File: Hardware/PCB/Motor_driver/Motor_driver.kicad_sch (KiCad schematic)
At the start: 87 parts, among them IC1 A89307KETSR-J, IC2 STM32L412KBT6, J1 ENCODER, J2 USB_C, J3 PAD_MOTEUR, J4 Debug, J5 Conn_01x01_Pin, J6 Conn_01x01_Pin, J7 Conn_01x01_Pin, J8 Conn_01x01_Pin

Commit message: update PCB, check driver BLDC
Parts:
- removed C22: 22µF, Capacitor_SMD:C_0603_1608Metric, symbol Device:C_Small
- removed C7, C8: 15µF, symbol Device:C_Polarized_Small
- removed D3: D_Zener 45V, symbol Device:D_Zener
- removed R1: 0.025, Resistor_SMD:R_0603_1608Metric, symbol Device:R
- removed R11, R13: 1, symbol Device:R
- removed R12, R14, R19, R20, R23: 0, symbol Device:R
- removed R21: 1k, symbol Device:R
- removed SQJ746ELP1, SQJ746ELP2, SQJ746ELP3: ~, Package_SO:PowerPAK_SO-8_Dual, symbol Custom:SQJ746ELP
- removed TP5: GATE C, TestPoint:TestPoint_Pad_D1.5mm, symbol Connector:TestPoint
- removed TP6: GATE B, TestPoint:TestPoint_Pad_D1.5mm, symbol Connector:TestPoint
- removed TP7: GATE A, TestPoint:TestPoint_Pad_D1.5mm, symbol Connector:TestPoint
- added J9: Conn_ST_STDC14, symbol Connector:Conn_ST_STDC14
- added R11: R_Shunt, symbol Device:R_Shunt
- C1, C2, C3: value 22µF -> 220n
- C15: value 4.7µF -> 4u7
- D1: MPN (none) -> 150060RS55040
- R2: value 200 -> 1k7
- R22: value 0 -> 10k; footprint (none) -> Resistor_SMD:R_0603_1608Metric
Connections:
- net +3.3V: now also R2.2, R22.2
- net GND: now also R11.4; no longer D1.1 (K), IC1.28 (SENN)
- net LSS: now also R11.1; no longer IC1.1 (SENP)
- net SA: no longer IC1.8 (SA), R22.2
- net SB: no longer IC1.10 (SB)
- net SC: no longer IC1.12 (SC)
- net arm_bridge_C/GHx: now reaches IC1.13 (GHC)
- net arm_bridge_A/GHx: now reaches IC1.9 (GHA)
- net at R22.1: now also D1.1 (K), IC1.26 (FAULT)
- net arm_bridge_B/GHx: now reaches IC1.11 (GHB)
- new net: J9.5 (GND), J9.7 (GND)
- new net SENN: IC1.28 (SENN), R11.3
- new net SENP: IC1.1 (SENP), R11.2
- new net arm_bridge_A/Sx: IC1.8 (SA)
- new net arm_bridge_B/Sx: IC1.10 (SB)
- new net arm_bridge_C/Sx: IC1.12 (SC)
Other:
- added sheet arm_bridge_A (arm_bridge.kicad_sch)
- added sheet arm_bridge_B (arm_bridge.kicad_sch)
- added sheet arm_bridge_C (arm_bridge.kicad_sch)
- moved on the sheet: C1, C2, C21, C3, D1, R2

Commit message: clean schematic
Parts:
- removed C17: 100nF, Capacitor_SMD:C_0603_1608Metric, symbol Device:C_Small
- removed IC2: STM32L412KBT6, SamacSys_Parts:QFP80P900X900X160-32N, symbol SamacSys_Parts:STM32L412KBT6
- removed J5, J6, J7, J8: Conn_01x01_Pin, MountingHole:MountingHole_3.2mm_M3_Pad_TopBottom, symbol Connector:Conn_01x01_Pin
- removed R17, R18, R6: 10k, Resistor_SMD:R_0603_1608Metric, symbol Device:R
- removed S1: 430181038816, SamacSys_Parts:430181038816, symbol SamacSys_Parts:430181038816
- removed TP10: BRAKE, TestPoint:TestPoint_Pad_D1.5mm, symbol Connector:TestPoint
- removed TP3: RX, TestPoint:TestPoint_Pad_D1.5mm, symbol Connector:TestPoint
- removed TP4: TX, TestPoint:TestPoint_Pad_D1.5mm, symbol Connector:TestPoint
- added H1, H2, H3, H4: MountingHole_Pad, symbol Mechanical:MountingHole_Pad
- added R1, R17: 10k, symbol Device:R_Small
- added R6: R_Small, symbol Device:R_Small
- added TP23: BRAKE, TestPoint:TestPoint_Pad_D1.5mm, symbol Connector:TestPoint
- added U2: STM32L412KBTx, Package_QFP:LQFP-32_7x7mm_P0.8mm, symbol MCU_ST_STM32L4:STM32L412KBTx
- C11: value 1µF -> 1u
- C12, C14, C4: value 4.7µF -> 4u7
- C13, C19: value 22µF -> 22u
- C16: value 100nF -> 100n
- C18: value 10µF -> 10u
- C20: value 15pF -> 15p
- C9: value 220µF -> 220u
- R3: value 5.6k -> 5k6
- renumbered Oscillator1 to Osc1
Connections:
- net +3.3V: now also J9.3 (VCC), R1.2, R17.1, R6.1, U2.1 (VDD), U2.17 (VDD), U2.5 (VDDA)
- net A: now also U2.6 (PA0)
- net B: now also U2.7 (PA1)
- net BRAKE: now also TP23.1, U2.13 (PA7)
- net DIR: now also U2.12 (PA6)
- net GND: now also J9.11 (GNDDetect), J9.5 (GND), J9.7 (GND), H1.1, H2.1, H3.1, H4.1, U2.16 (VSS), U2.32 (VSS)
- net GPIO3: now also U2.10 (PA4)
- net PA11: now also U2.21 (PA11)
- net PWM: now also U2.11 (PA5)
- net RX: now also U2.30 (PB7)
- net SCL: now also R15.1, TP1.1, U2.19 (PA9); no longer R16.1, TP2.1
- net SDA: now also R16.1, TP2.1, U2.20 (PA10); no longer R15.1, TP1.1
- net SWCLK: now also U2.24 (PA14)
- net SWDIO: now also U2.23 (PA13)
- net SWO: now also U2.26 (PB3)
- net TX: now also U2.29 (PB6)
- net X: now also U2.9 (PA3)
- net at S3.1: now also R1.1
- net at S3.3 (2): now also U2.15 (PB1)
- net at S3.4 (1): now also U2.14 (PB0)
- net at S3.2: now also R17.2
- new net: R6.2, U2.4 (NRST)
- no-connect marks 16 -> 10
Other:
- moved on the sheet: C1, C10, C11, C12, C13, C14, C15, C16, C18, C19, C2, C20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

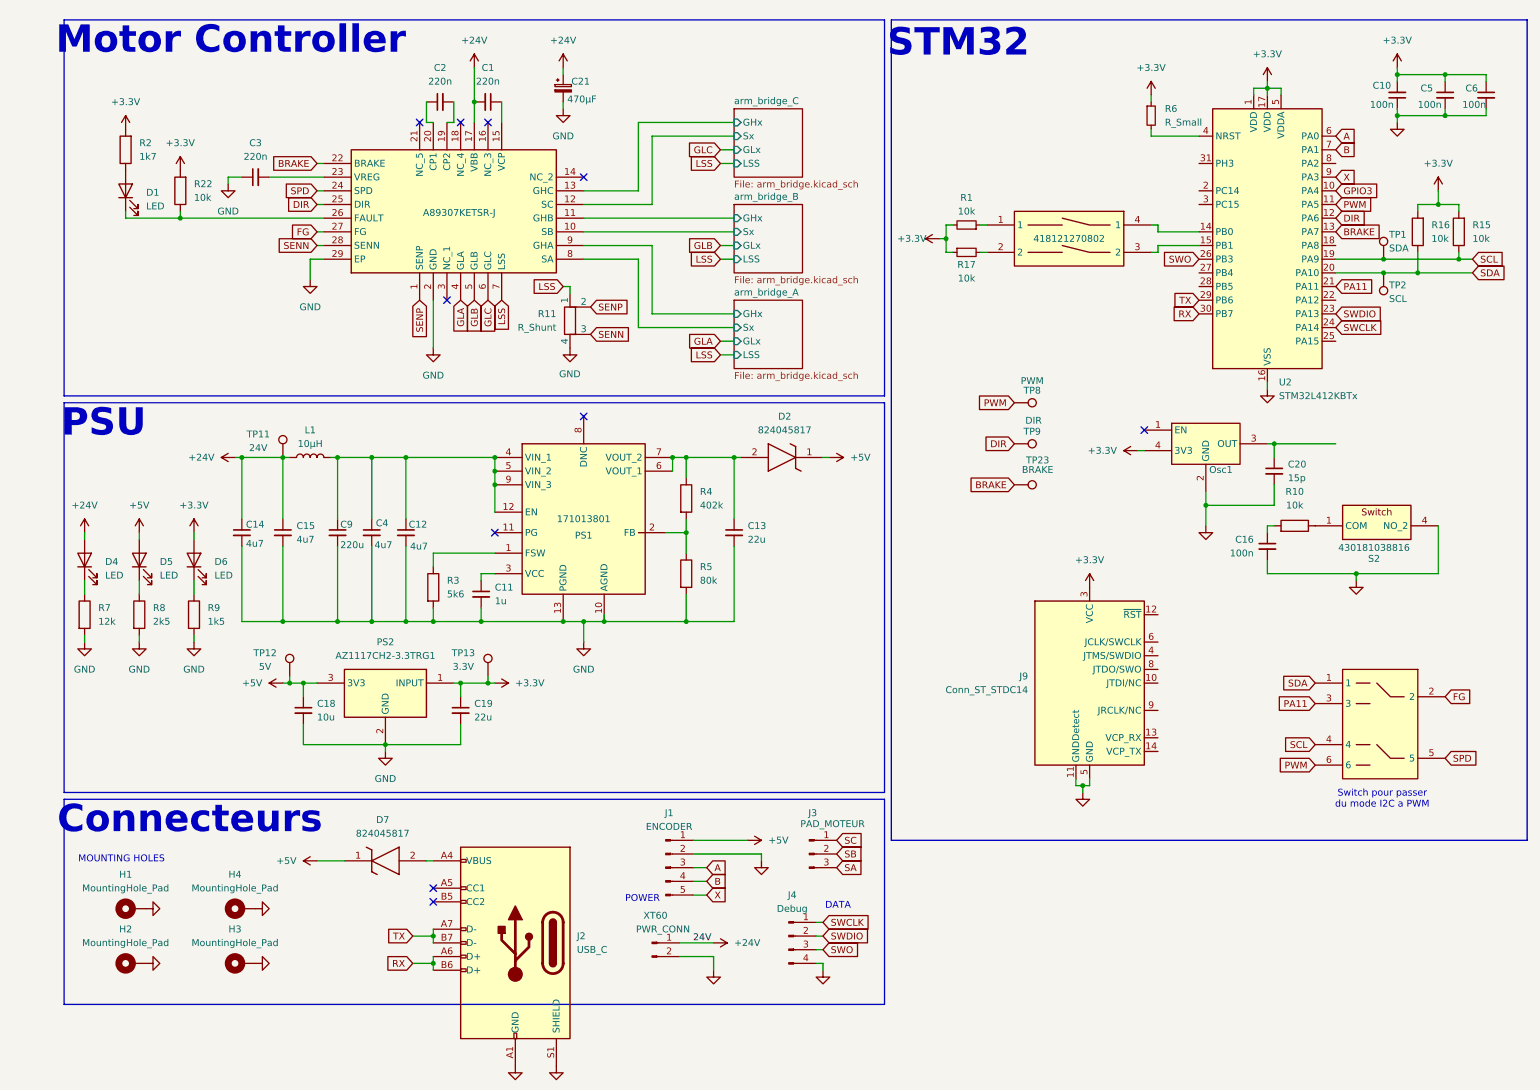
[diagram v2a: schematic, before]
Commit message: update schematic
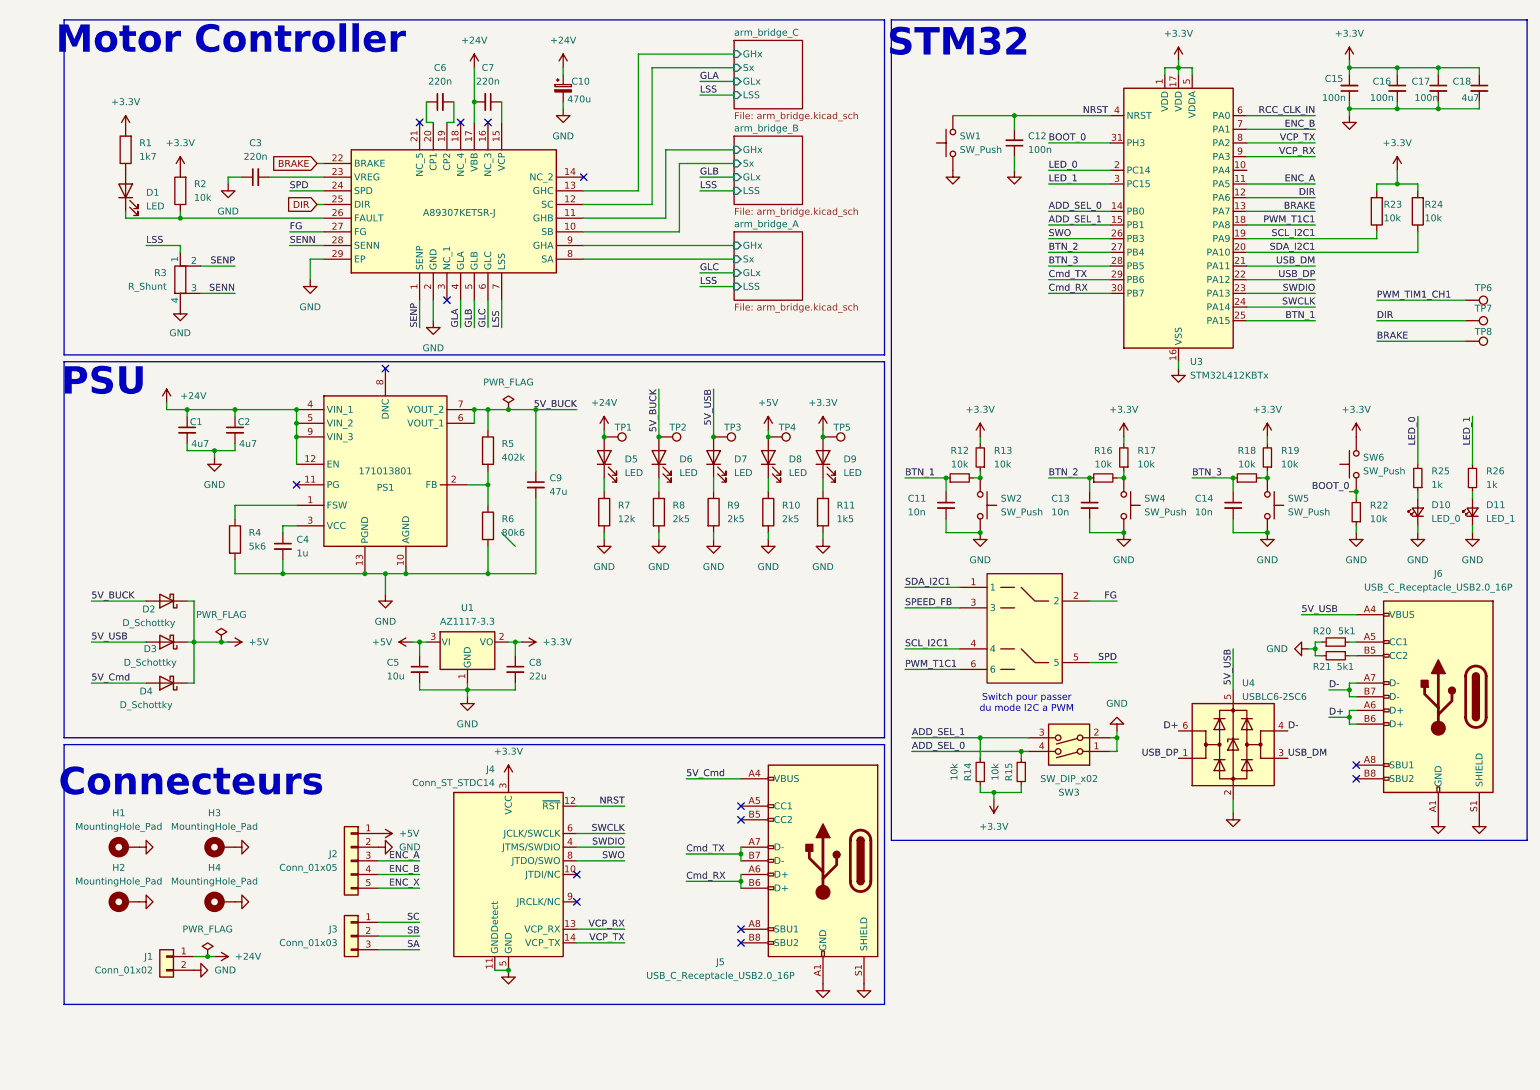
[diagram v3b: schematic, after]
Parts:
- removed C15, C4: 4u7, Capacitor_SMD:C_0603_1608Metric, symbol Device:C_Small
- removed C16: 100n, Capacitor_SMD:C_0603_1608Metric, symbol Device:C_Small
- removed C20: 15p, Capacitor_SMD:C_0603_1608Metric, symbol Device:C_Small
- removed C9: 220u, Capacitor_SMD:C_0603_1608Metric, symbol Device:C_Small
- removed D2, D7: 824045817, SamacSys_Parts:824045817, symbol SamacSys_Parts:824045817
- removed J1: ENCODER, Connector_JST:JST_SH_SM05B-SRSS-TB_1x05-1MP_P1.00mm_Horizontal, symbol Connector:Conn_01x05_Pin
- removed J2: USB_C, Connector_USB:USB_C_Receptacle_GCT_USB4105-xx-A_16P_TopMnt_Horizontal, symbol Connector:USB_C_Receptacle_USB2.0_14P
- removed J3: PAD_MOTEUR, Custom:Solder Pad x3, symbol Connector:Conn_01x03_Pin
- removed J4: Debug, Connector_JST:JST_SH_SM04B-SRSS-TB_1x04-1MP_P1.00mm_Horizontal, symbol Connector:Conn_01x04_Pin
- removed L1: 10µH, SamacSys_Parts:WE-MAPI_3020, symbol Device:L
- removed Osc1: ~, Custom:Oscillator 7x5mm, symbol Custom:Oscillator_831018577
- removed PS2: AZ1117CH2-3.3TRG1, SamacSys_Parts:SOT230P700X180-4N, symbol SamacSys_Parts:AZ1117CH2-3.3TRG1
- removed R1: 10k, symbol Device:R_Small
- removed R6: R_Small, symbol Device:R_Small
- removed S2: 430181038816, SamacSys_Parts:430181038816, symbol SamacSys_Parts:430181038816
- removed S3: 418121270802, SamacSys_Parts:418121270802, symbol SamacSys_Parts:418121270802
- removed TP11: 24V, TestPoint:TestPoint_Pad_D1.5mm, symbol Connector:TestPoint
- removed TP2: SCL, TestPoint:TestPoint_Pad_D1.5mm, symbol Connector:TestPoint
- removed XT60: PWR_CONN, Connector_AMASS:AMASS_XT60PW-M_1x02_P7.20mm_Horizontal, symbol Connector:Conn_01x02_Pin
- added C1: 4u7, Capacitor_SMD:C_1210_3225Metric, symbol Device:C_Small
- added C11, C13: 10n, Capacitor_SMD:C_0402_1005Metric, symbol Device:C_Small
- added C12: 100n, Capacitor_SMD:C_0402_1005Metric, symbol Device:C_Small
- added C18: 4u7, Capacitor_SMD:C_0603_1608Metric, symbol Device:C_Small
- added D10: LED_0, LED_SMD:LED_0603_1608Metric, symbol Device:LED_Small
- added D11: LED_1, LED_SMD:LED_0603_1608Metric, symbol Device:LED_Small
- added D2, D3, D4: D_Schottky, symbol Device:D_Schottky
- added D7, D8: LED, LED_SMD:LED_0603_1608Metric, symbol Device:LED
- added J1: Conn_01x02, symbol Connector_Generic:Conn_01x02
- added J2: Conn_01x05, symbol Connector_Generic:Conn_01x05
- added J3: Conn_01x03, symbol Connector_Generic:Conn_01x03
- added J5, J6: USB_C_Receptacle_USB2.0_16P, symbol Connector:USB_C_Receptacle_USB2.0_16P
- added R12, R13, R14, R16, R17, R18, R19, R22: 10k, Resistor_SMD:R_0402_1005Metric, symbol Device:R_Small
- added R20, R21: 5k1, Resistor_SMD:R_0402_1005Metric, symbol Device:R_Small
- added R25, R26: 1k, Resistor_SMD:R_0402_1005Metric, symbol Device:R_Small
- added R9: 2k5, Resistor_SMD:R_0402_1005Metric, symbol Device:R
- added SW1, SW2, SW4, SW5, SW6: SW_Push, symbol Switch:SW_Push
- added SW3: SW_DIP_x02, symbol Switch:SW_DIP_x02
- added TP3: 5V_USB, TestPoint:TestPoint_Pad_D1.0mm, symbol Connector:TestPoint
- added TP4: 5V, TestPoint:TestPoint_Pad_D1.0mm, symbol Connector:TestPoint
- added U1: AZ1117-3.3, symbol Regulator_Linear:AZ1117-3.3
- added U4: USBLC6-2SC6, Package_TO_SOT_SMD:SOT-23-6, symbol Power_Protection:USBLC6-2SC6
- C10: renamed from C21; value 470µF -> 470u
- C14: value 4u7 -> 10n; footprint Capacitor_SMD:C_0603_1608Metric -> Capacitor_SMD:C_0402_1005Metric; MPN (none) -> WE 885012205050
- C15: renamed from C10; footprint Capacitor_SMD:C_0603_1608Metric -> Capacitor_SMD:C_0402_1005Metric
- C16: renamed from C5; footprint Capacitor_SMD:C_0603_1608Metric -> Capacitor_SMD:C_0402_1005Metric
- C17: renamed from C6; footprint Capacitor_SMD:C_0603_1608Metric -> Capacitor_SMD:C_0402_1005Metric
- C2: renamed from C12; footprint Capacitor_SMD:C_0603_1608Metric -> Capacitor_SMD:C_1210_3225Metric; MPN (none) -> 885012209048; Vmax (none) -> 50V
- C3: footprint Capacitor_SMD:C_0603_1608Metric -> Capacitor_SMD:C_0402_1005Metric
- C4: renamed from C11; MPN (none) -> 885012207051
- C6: renamed from C2; footprint Capacitor_SMD:C_0603_1608Metric -> Capacitor_SMD:C_0402_1005Metric
- C7: renamed from C1; footprint Capacitor_SMD:C_0603_1608Metric -> Capacitor_SMD:C_0402_1005Metric
- C9: renamed from C13; value 22u -> 47u
- D5: renamed from D4; footprint Capacitor_SMD:C_0603_1608Metric -> LED_SMD:LED_0603_1608Metric
- D6: renamed from D5; footprint Capacitor_SMD:C_0603_1608Metric -> LED_SMD:LED_0603_1608Metric
- D9: renamed from D6; footprint Capacitor_SMD:C_0603_1608Metric -> LED_SMD:LED_0603_1608Metric
- H1, H2: footprint (none) -> MountingHole:MountingHole_3.2mm_M3_Pad_Via
- H3: renamed from H4; footprint (none) -> MountingHole:MountingHole_3.2mm_M3_Pad_Via
- H4: renamed from H3; footprint (none) -> MountingHole:MountingHole_3.2mm_M3_Pad_Via
- R1: renamed from R2; footprint Resistor_SMD:R_0603_1608Metric -> Resistor_SMD:R_0402_1005Metric
- R10: value 10k -> 2k5; footprint Resistor_SMD:R_0603_1608Metric -> Resistor_SMD:R_0402_1005Metric
- R11: renamed from R9; footprint Resistor_SMD:R_0603_1608Metric -> Resistor_SMD:R_0402_1005Metric
- R15: renamed from R17; footprint (none) -> Resistor_SMD:R_0402_1005Metric
- R2: renamed from R22; footprint Resistor_SMD:R_0603_1608Metric -> Resistor_SMD:R_0402_1005Metric
- R23: renamed from R15; footprint Resistor_SMD:R_0603_1608Metric -> Resistor_SMD:R_0402_1005Metric
- R24: renamed from R16; footprint Resistor_SMD:R_0603_1608Metric -> Resistor_SMD:R_0402_1005Metric
- R4: renamed from R3; footprint Resistor_SMD:R_0603_1608Metric -> Resistor_SMD:R_0402_1005Metric
- R5: renamed from R4; footprint Resistor_SMD:R_0603_1608Metric -> Resistor_SMD:R_0402_1005Metric
- R6: renamed from R5; value 80k -> 80k6; footprint Resistor_SMD:R_0603_1608Metric -> Resistor_SMD:R_0402_1005Metric
- R7, R8: footprint Resistor_SMD:R_0603_1608Metric -> Resistor_SMD:R_0402_1005Metric
- TP1: value SDA -> 24V; footprint TestPoint:TestPoint_Pad_D1.5mm -> TestPoint:TestPoint_Pad_D1.0mm
- TP2: renamed from TP12; value 5V -> 5V_BUCK; footprint TestPoint:TestPoint_Pad_D1.5mm -> TestPoint:TestPoint_Pad_D1.0mm
- TP5: renamed from TP13; value 3.3V -> 3V3; footprint TestPoint:TestPoint_Pad_D1.5mm -> TestPoint:TestPoint_Pad_D1.0mm
- TP6: renamed from TP8; footprint TestPoint:TestPoint_Pad_D1.5mm -> TestPoint:TestPoint_Pad_D1.0mm
- TP7: renamed from TP9; footprint TestPoint:TestPoint_Pad_D1.5mm -> TestPoint:TestPoint_Pad_D1.0mm
- TP8: renamed from TP23; footprint TestPoint:TestPoint_Pad_D1.5mm -> TestPoint:TestPoint_Pad_D1.0mm
- renumbered C18 to C5, C19 to C8, J9 to J4, R11 to R3, U1 to U2, U2 to U3
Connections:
- net X is gone; now on net VCP_RX: U3.9 (PA3)
- net +24V: now also C2.1, PS1.12 (EN), PS1.4 (VIN_1), PS1.5 (VIN_2), PS1.9 (VIN_3), TP1.1, C1.1, J1.1 (Pin_1); no longer C14.1
- net +3.3V: now also R15.2, C18.1, R13.2, R14.2, R17.2, R19.2, SW6.2, U1.2 (VO); no longer R15.1
- net +5V: now also D2.1 (K), D3.1 (K), D4.1 (K), D8.2 (A), J2.1 (Pin_1), TP4.1, U1.3 (VI); no longer D6.2 (A), TP2.1
- net GND: now also R10.2, C1.2, C11.2, C12.1, C13.2, C18.2, D10.1 (K), D11.1 (K), J1.2 (Pin_2), J2.2 (Pin_2), J5.A1 (GND), J5.A12 (GND), J5.B1 (GND), J5.B12 (GND), J5.S1 (SHIELD), J6.A1 (GND), J6.A12 (GND), J6.B1 (GND), J6.B12 (GND), J6.S1 (SHIELD), R20.1, R21.2, R22.1, R9.2, SW1.1, SW2.2, SW3.1, SW3.2, SW4.2, SW5.2, U1.1 (GND), U4.2 (GND)
- net SA: now also J3.3 (Pin_3)
- net SB: now also J3.2 (Pin_2)
- net SC: now also J3.1 (Pin_1)
- net SWCLK: now also J4.6 (JCLK/SWCLK)
- net SWDIO: now also J4.4 (JTMS/SWDIO)
- net SWO: now also J4.8 (JTDO/SWO)
- net 5V_BUCK: now reaches C9.1, PS1.6 (VOUT_1), PS1.7 (VOUT_2), R5.1
- net 5V_BUCK: now also D6.2 (A), TP2.1, D2.2 (A)
- net at R10.1: now also D8.1 (K)
- net NRST: now reaches J4.12 (~{RST})
- net NRST: now also U3.4 (NRST), C12.2, SW1.2
- net VCP_RX: now reaches J4.13 (VCP_RX)
- net VCP_TX: now reaches J4.14 (VCP_TX)
- net VCP_TX: now also U3.8 (PA2)
- net ADD_SEL_1: now reaches U3.15 (PB1)
- net ADD_SEL_1: now also R14.1, SW3.3
- net ADD_SEL_0: now reaches U3.14 (PB0)
- net ADD_SEL_0: now also R15.1, SW3.4
- net PWM_T1C1: now reaches U3.18 (PA8)
- net PWM_T1C1: now also U2.6
- net LED_0: now reaches U3.2 (PC14)
- net LED_0: now also R25.2
- net USB_DP: now reaches U3.22 (PA12)
- net USB_DP: now also U4.1 (I/O1)
- net BTN_1: now reaches U3.25 (PA15)
- net BTN_1: now also C11.1, R12.1
- net BTN_2: now reaches U3.27 (PB4)
- net BTN_2: now also C13.1, R16.1
- net BTN_3: now reaches U3.28 (PB5)
- net BTN_3: now also C14.1, R18.1
- net LED_1: now reaches U3.3 (PC15)
- net LED_1: now also R26.2
- net BOOT_0: now reaches U3.31 (PH3)
- net BOOT_0: now also R22.2, SW6.1
- net A renamed RCC_CLK_IN
- net B renamed ENC_B
- net ENC_B: now also J2.4 (Pin_4)
- net GPIO3: no longer names the net of U3.10 (PA4)
- net PA11 renamed SPEED_FB
- net SPEED_FB: no longer U3.21 (PA11)
- removed net PWM: TP6.1, U2.6, U3.11 (PA5)
- net RX renamed Cmd_RX
- net Cmd_RX: now also J5.A6 (D+), J5.B6 (D+)
- net SCL renamed SCL_I2C1
- net SCL_I2C1: no longer TP1.1
- net SDA renamed SDA_I2C1
- net TX renamed Cmd_TX
- net Cmd_TX: now also J5.A7 (D-), J5.B7 (D-)
- new net: D10.2 (A), R25.1
- new net: R12.2, R13.1, SW2.1
- new net: J6.A5 (CC1), R20.2
- new net: R18.2, R19.1, SW5.1
- new net: D7.1 (K), R9.1
- new net: R16.2, R17.1, SW4.1
- new net: D11.2 (A), R26.1
- new net: J6.B5 (CC2), R21.1
- new net 5V_Cmd: D4.2 (A), J5.A4 (VBUS), J5.A9 (VBUS), J5.B4 (VBUS), J5.B9 (VBUS)
- new net 5V_USB: D3.2 (A), D7.2 (A), J6.A4 (VBUS), J6.A9 (VBUS), J6.B4 (VBUS), J6.B9 (VBUS), TP3.1, U4.5 (VBUS)
- new net D+: J6.A6 (D+), J6.B6 (D+), U4.6 (I/O1)
- new net D-: J6.A7 (D-), J6.B7 (D-), U4.4 (I/O2)
- new net ENC_A: J2.3 (Pin_3), U3.11 (PA5)
- new net ENC_X: J2.5 (Pin_5)
- new net PWM_TIM1_CH1: TP6.1
- new net USB_DM: U3.21 (PA11), U4.3 (I/O2)
- no-connect marks 10 -> 15
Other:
- note removed: "DATA"
- note removed: "MOUNTING HOLES"
- note removed: "POWER"
- moved on the sheet: C15, C16, C17, C2, C4, C5, C8, C9, D5, D6, D9, H1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

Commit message: update
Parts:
- J4: footprint (none) -> Connector_PinHeader_1.27mm:PinHeader_2x07_P1.27mm_Vertical_SMD
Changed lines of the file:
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@@
 		(at 138.43 158.75)
 	)
-	(bus_entry
-		(at 93.98 107.95)
-		(size 2.54 2.54)
-		(stroke
-			(width 0)
-			(type default)
-		)
-	)
 	(wire
 		(pts
@@
 			)
 		)
-		(property "Footprint" ""
+		(property "Footprint" "Connector_PinHeader_1.27mm:PinHeader_2x07_P1.27mm_Vertical_SMD"
 			(at 95.25 171.45 0)
 			(effects
